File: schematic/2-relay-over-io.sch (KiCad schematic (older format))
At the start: 25 parts, among them J1 WJ142R-5.08-3P, J2 WJ142R-5.08-3P, J5 Conn_02x05_Odd_Even, J6 Conn_02x05_Odd_Even, J7 Conn_02x08_Odd_Even, J8 Conn_02x08_Odd_Even, Q2 BC817, Q3 BC817, U1 SONGLE_3V_relay, U2 SONGLE_3V_relay, U6 DizzyBITLogo, U7 DizzyBIT-Layout

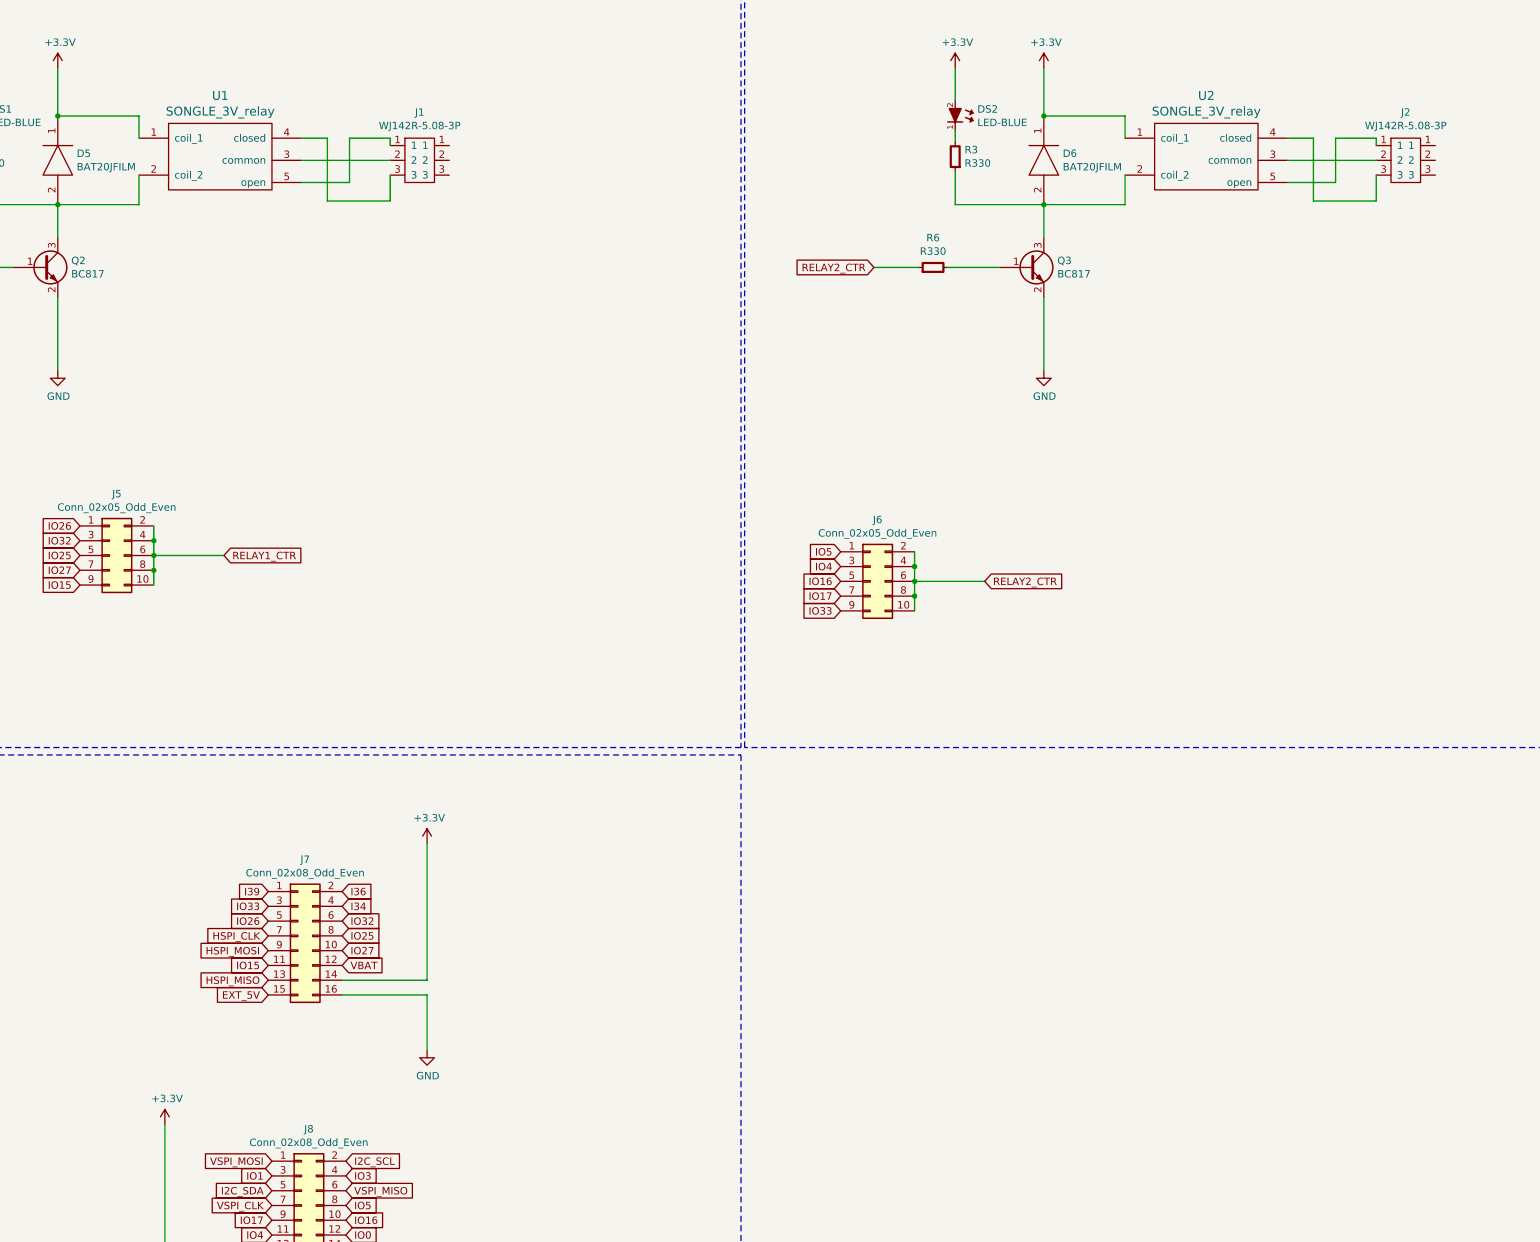
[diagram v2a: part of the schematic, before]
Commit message: Changed Connector designators
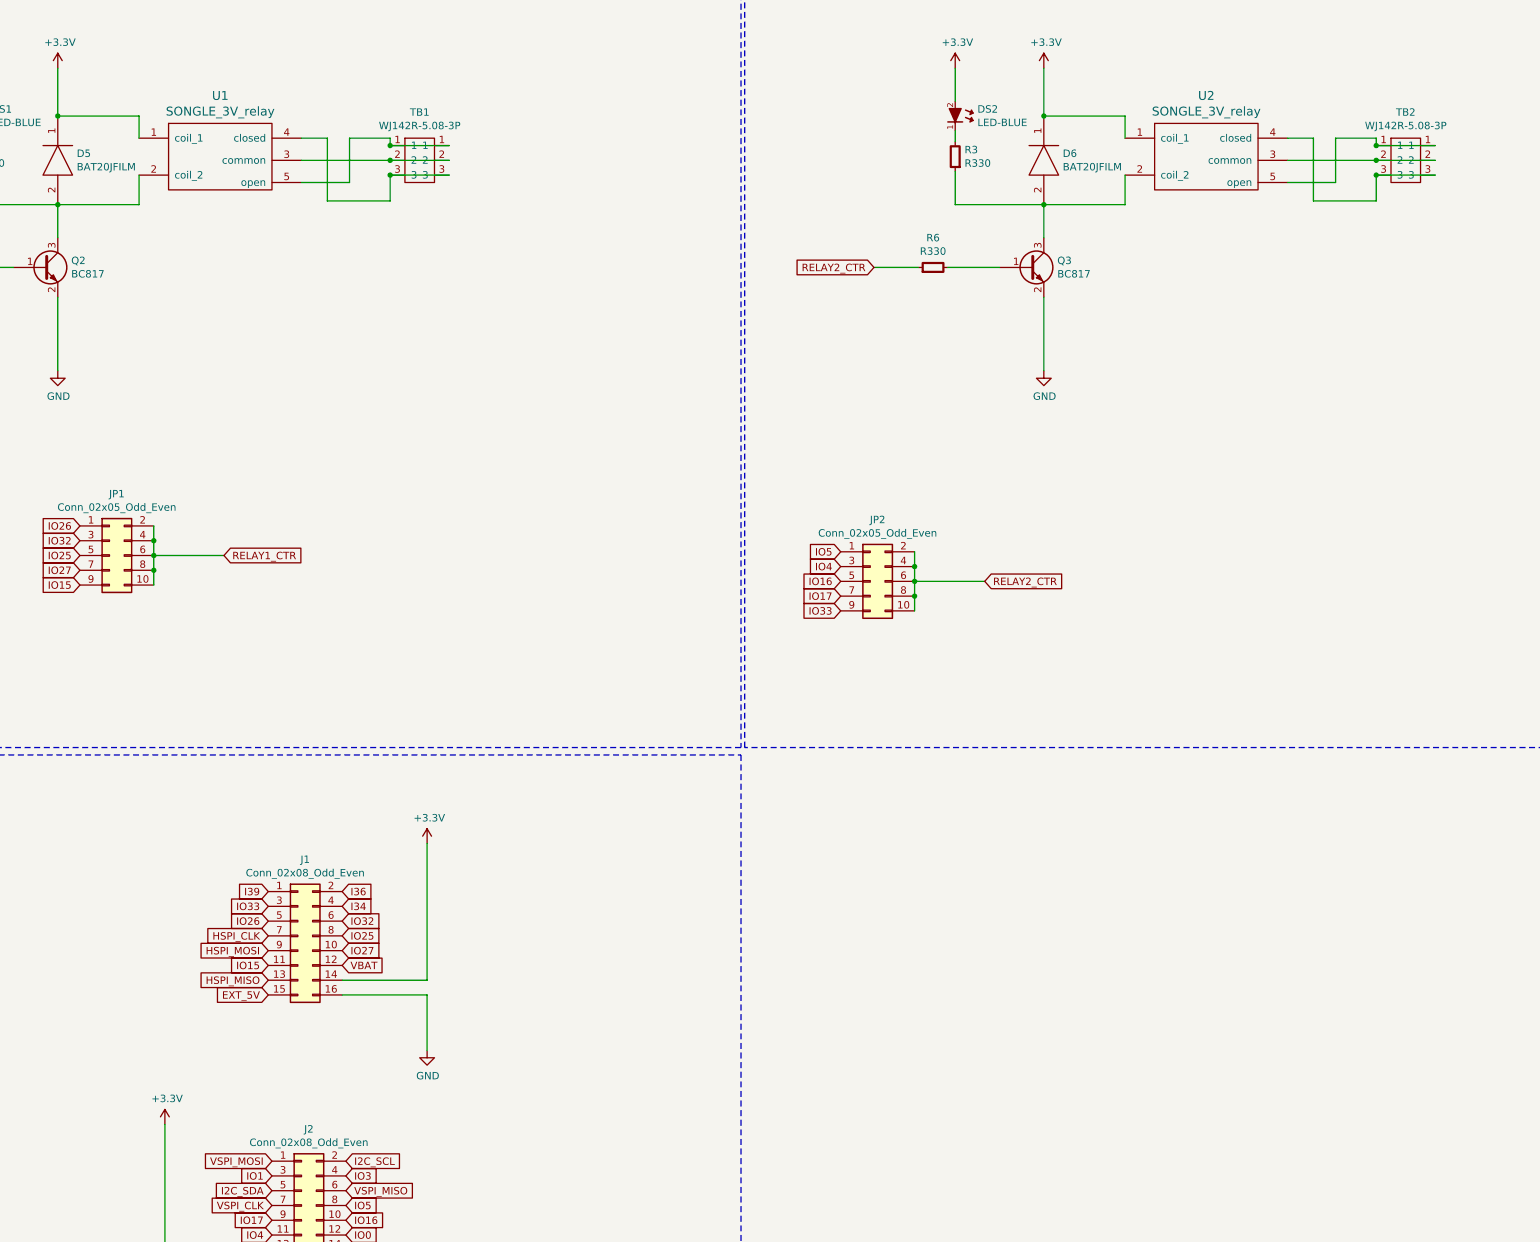
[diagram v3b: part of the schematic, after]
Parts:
- renumbered J7 to J1, J8 to J2, J5 to JP1, J6 to JP2, J1 to TB1, J2 to TB2
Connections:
- net at TB2.1: now also U2.5 (open)
- net at TB2.2: now also U2.3 (common)
- net at TB2.3: now also U2.4 (closed)
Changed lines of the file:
@@
 VSPI_MOSI
 $Comp
-L Connector_Generic:Conn_02x08_Odd_Even J7
+L Connector_Generic:Conn_02x08_Odd_Even J1
 U 1 1 5D8B59AB
 P 4250 7600
-F 0 "J7" H 4300 8117 50  0000 C CNN
+F 0 "J1" H 4300 8117 50  0000 C CNN
 F 1 "Conn_02x08_Odd_Even" H 4300 8026 50  0000 C CNN
 F 2 "Connector_PinHeader_2.54mm:PinHeader_2x08_P2.54mm_Vertical" H 4250 7600 50  0001 C CNN
@@
 $EndComp
 $Comp
-L Connector_Generic:Conn_02x08_Odd_Even J8
+L Connector_Generic:Conn_02x08_Odd_Even J2
 U 1 1 5D8FF691
 P 4275 9425
-F 0 "J8" H 4325 9942 50  0000 C CNN
+F 0 "J2" H 4325 9942 50  0000 C CNN
 F 1 "Conn_02x08_Odd_Even" H 4325 9851 50  0000 C CNN
 F 2 "Connector_PinHeader_2.54mm:PinHeader_2x08_P2.54mm_Vertical" H 4275 9425 50  0001 C CNN
@@
 	9300 3775 9300 3275
 $Comp
-L Connector_Generic:Conn_02x05_Odd_Even J5
+L Connector_Generic:Conn_02x05_Odd_Even JP1
 U 1 1 5D99A860
 P 2975 5025
-F 0 "J5" H 3025 5442 50  0000 C CNN
+F 0 "JP1" H 3025 5442 50  0000 C CNN
 F 1 "Conn_02x05_Odd_Even" H 3025 5351 50  0000 C CNN
 F 2 "DizzyBit:DizzyBit-SolderJumper-5-5-Open" H 2975 5025 50  0001 C CNN
@@
 IO15
 $Comp
-L Connector_Generic:Conn_02x05_Odd_Even J6
+L Connector_Generic:Conn_02x05_Odd_Even JP2
 U 1 1 5D9C15BE
 P 8125 5200
-F 0 "J6" H 8175 5617 50  0000 C CNN
+F 0 "JP2" H 8175 5617 50  0000 C CNN
 F 1 "Conn_02x05_Odd_Even" H 8175 5526 50  0000 C CNN
 F 2 "DizzyBit:DizzyBit-SolderJumper-5-5-Open" H 8125 5200 50  0001 C CNN
@@
 IO33
 $Comp
-L Connector_Generic:WJ142R-5.08-3P J1
+L Connector_Generic:WJ142R-5.08-3P TB1
 U 1 1 5D93C8FC
 P 4975 2150
-F 0 "J1" H 5075 2275 50  0000 C CNN
+F 0 "TB1" H 5075 2275 50  0000 C CNN
 F 1 "WJ142R-5.08-3P" H 5075 2184 50  0000 C CNN
 F 2 "TerminalBlock:WJ142R-5.08-3P" H 4975 2150 50  0001 C CNN
@@
 $EndComp
 $Comp
-L Connector_Generic:WJ142R-5.08-3P J2
+L Connector_Generic:WJ142R-5.08-3P TB2
 U 1 1 5D93CB98
 P 11650 2150
-F 0 "J2" H 11750 2275 50  0000 C CNN
+F 0 "TB2" H 11750 2275 50  0000 C CNN
 F 1 "WJ142R-5.08-3P" H 11750 2184 50  0000 C CNN
 F 2 "TerminalBlock:WJ142R-5.08-3P" H 11650 2150 50  0001 C CNN
@@
 Wire Wire Line
 	5125 7900 4550 7900
+Wire Wire Line
+	4875 2250 5275 2250
+Connection ~ 4875 2250
+Wire Wire Line
+	4875 2350 5275 2350
+Connection ~ 4875 2350
+Wire Wire Line
+	4875 2450 5275 2450
+Connection ~ 4875 2450
+Wire Wire Line
+	11550 2250 11950 2250
+Connection ~ 11550 2250
+Wire Wire Line
+	11950 2350 11550 2350
+Connection ~ 11550 2350
+Wire Wire Line
+	11550 2450 11950 2450
+Connection ~ 11550 2450
 $EndSCHEMATC

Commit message: Changed the relay footprint to have bigger holes
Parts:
- U1, U2: footprint Songle:SONGLE_5V_Relay -> Songle:SONGLE_3V_Relay
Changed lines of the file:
@@
 F 0 "U1" H 3725 2787 60  0000 C CNN
 F 1 "SONGLE_3V_relay" H 3725 2681 60  0000 C CNN
-F 2 "Songle:SONGLE_5V_Relay" H 3875 2350 60  0001 C CNN
+F 2 "Songle:SONGLE_3V_Relay" H 3875 2350 60  0001 C CNN
 F 3 "https://datasheet.lcsc.com/szlcsc/Ningbo-Songle-Relay-SRD-03VDC-SL-C-blue_C24585.pdf" H 3875 2350 60  0001 C CNN
 F 4 "SRD-03VDC-SL-C" H 3725 2350 50  0001 C CNN "pn"
@@
 F 0 "U2" H 10400 2787 60  0000 C CNN
 F 1 "SONGLE_3V_relay" H 10400 2681 60  0000 C CNN
-F 2 "Songle:SONGLE_5V_Relay" H 10550 2350 60  0001 C CNN
+F 2 "Songle:SONGLE_3V_Relay" H 10550 2350 60  0001 C CNN
 F 3 "https://datasheet.lcsc.com/szlcsc/Ningbo-Songle-Relay-SRD-03VDC-SL-C-blue_C24585.pdf" H 10550 2350 60  0001 C CNN
 F 4 "SRD-03VDC-SL-C" H 10400 2350 50  0001 C CNN "pn"
